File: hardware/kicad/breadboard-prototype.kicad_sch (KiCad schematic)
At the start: 12 parts, among them J1 nRF52 DK PCA10040 interface, J2 Waveshare 2.13inch HAT Rev2.1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, J3 Adafruit LIS3DH breakout, J4 DCF-1060N-800 (PON active-low), Q1 2N3904

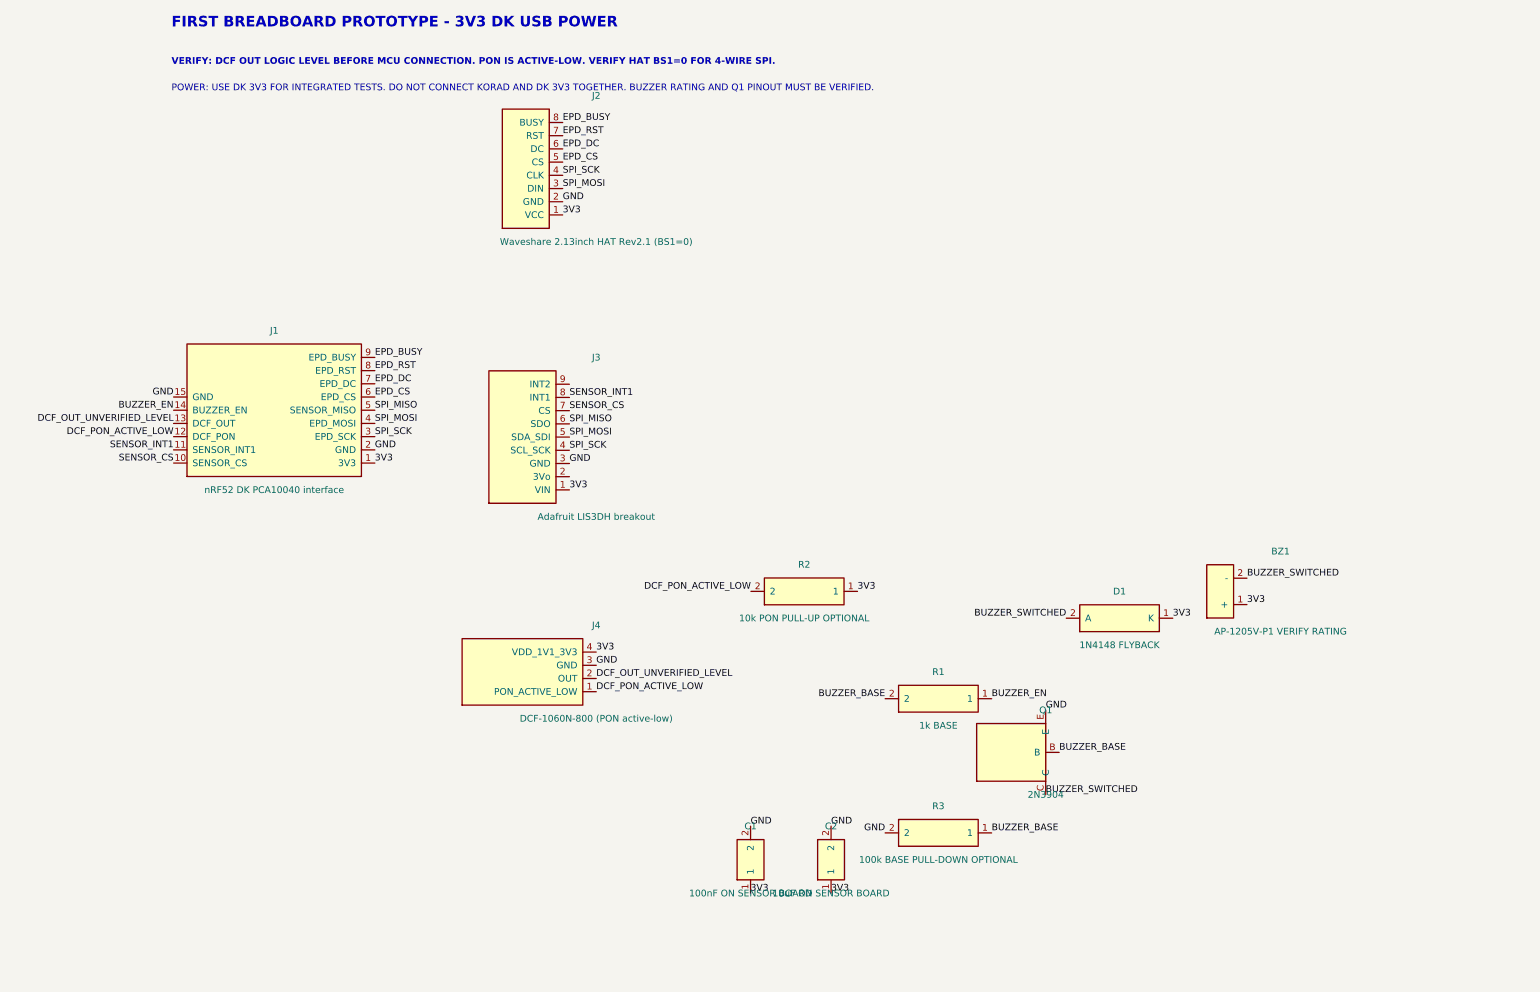
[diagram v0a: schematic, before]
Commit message: hardware: wire breadboard prototype modules
Add visible orthogonal wiring for module interfaces, DCF control,\nand the transistor-driven buzzer circuit.
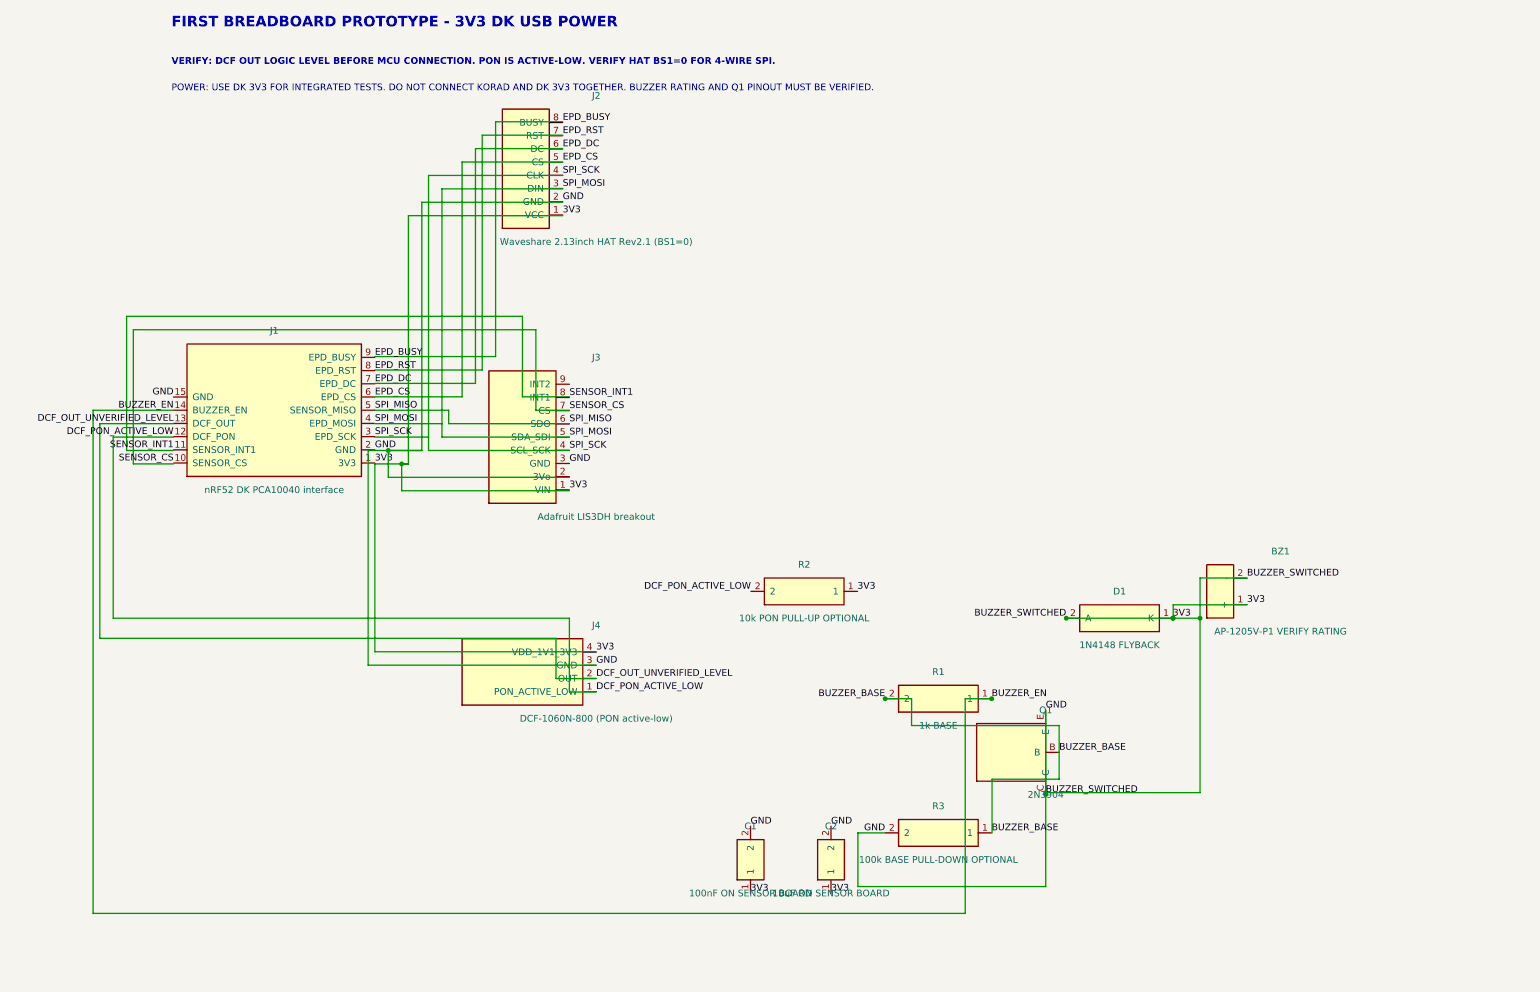
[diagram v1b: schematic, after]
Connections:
- net BUZZER_SWITCHED is gone; now on net 3V3: BZ1.2 (-), D1.2 (A), Q1.C

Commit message: hardware: tidy breadboard schematic layout
Rearrange modules into functional blocks, remove crossing routes,\nand export a reviewed PDF with cleaner display and buzzer wiring.
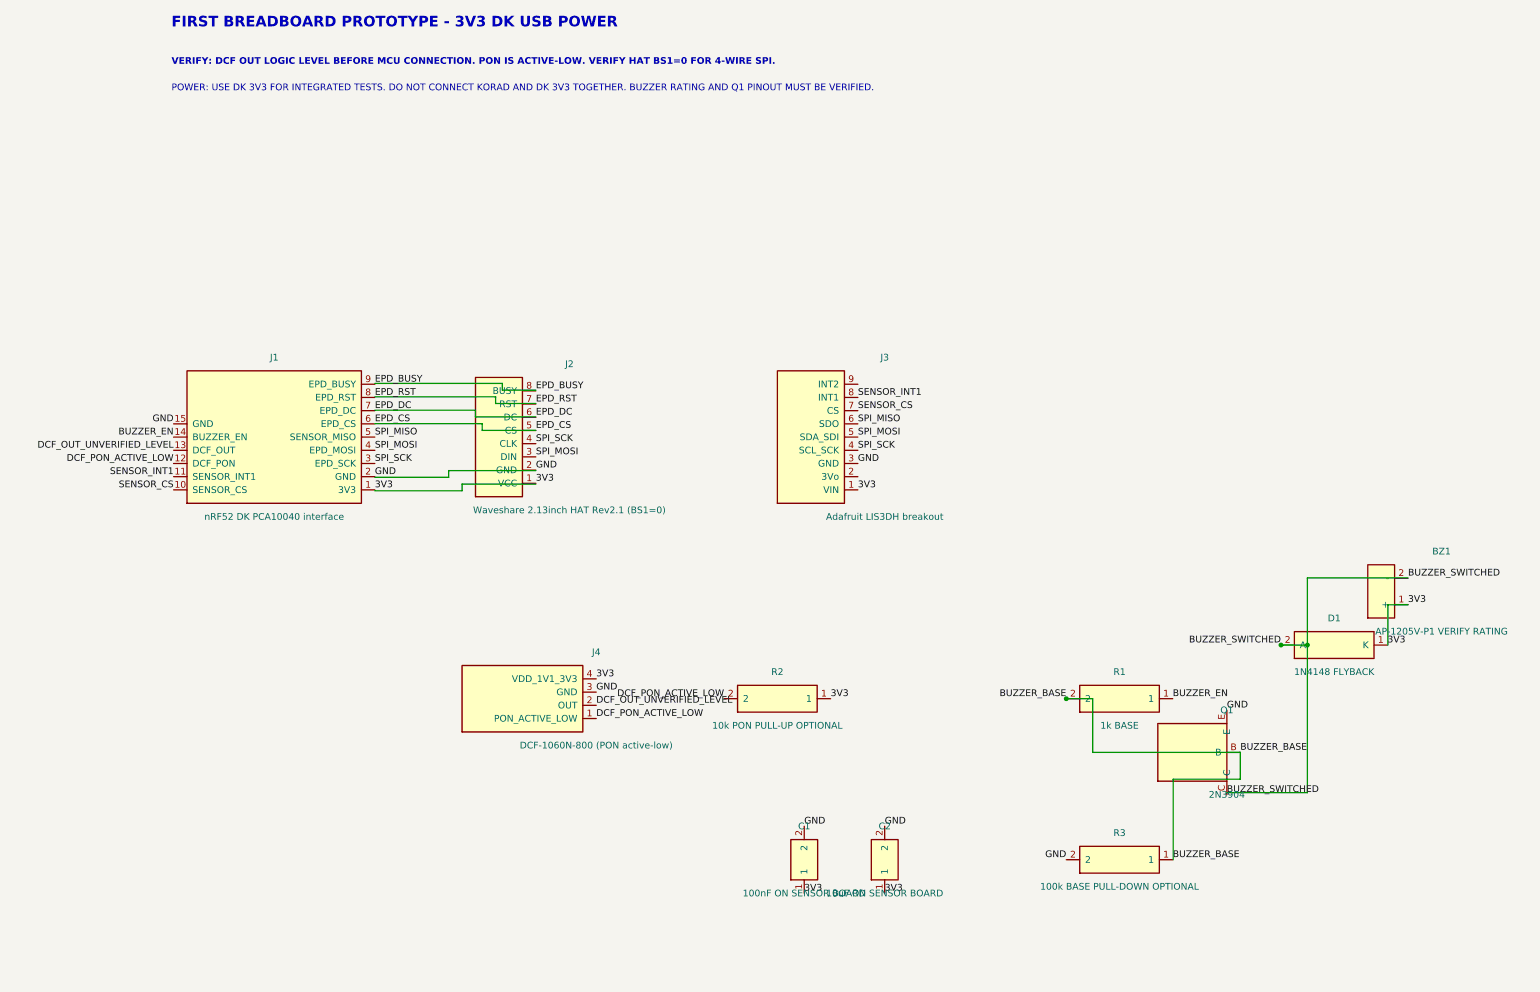
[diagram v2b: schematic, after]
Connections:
- net 3V3: no longer BZ1.2 (-), D1.2 (A), Q1.C
- new net BUZZER_SWITCHED: BZ1.2 (-), D1.2 (A), Q1.C
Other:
- moved on the sheet: BZ1, C1, C2, D1, J1, J2, J3, J4, Q1, R1, R2, R3

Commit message: hardware: modularize and clean breadboard schematic layout
Restructure schematic into five clearly demarcated functional blocks:
- Block 1: Host MCU Interface (nRF52 DK / PCA10040)
- Block 2: Display Interface (Waveshare 2.13" HAT Rev2.1)
- Block 3: Motion Sensor (Adafruit LIS3DH #2809) with decoupling
- Block 4: Time Sync (DCF-1060N-800) with PON pull-up and voltage caution
- Block 5: Transistor Buzzer Driver (2N3904 + 1N4148 + AP-1205V-P1)
- Block 6: Safety rules, boot safe states, and staged bring-up guide

Rebuild custom symbols on a strict 2.54 mm grid, register official KiCad
Device and power symbol libraries, eliminate long crossing wires, and export
reviewed PDF.
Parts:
- removed BZ1: AP-1205V-P1 VERIFY RATING, symbol BreadboardPrototype:Buzzer
- removed C1: 100nF ON SENSOR BOARD, symbol BreadboardPrototype:Capacitor
- removed C2: 10uF ON SENSOR BOARD, symbol BreadboardPrototype:Capacitor
- removed D1: 1N4148 FLYBACK, symbol BreadboardPrototype:Diode
- removed J1: nRF52 DK PCA10040 interface, symbol BreadboardPrototype:DK_Interface
- removed J2: Waveshare 2.13inch HAT Rev2.1 (BS1=0), symbol BreadboardPrototype:Epaper_HAT
- removed J3: Adafruit LIS3DH breakout, symbol BreadboardPrototype:LIS3DH_Breakout
- removed Q1: 2N3904, symbol BreadboardPrototype:NPN_2N3904
- removed R1: 1k BASE, symbol BreadboardPrototype:Resistor
- removed R2: 10k PON PULL-UP OPTIONAL, symbol BreadboardPrototype:Resistor
- removed R3: 100k BASE PULL-DOWN OPTIONAL, symbol BreadboardPrototype:Resistor
- added BZ1: AP-1205V-P1, symbol Device:Buzzer
- added C1: 100nF, symbol Device:C
- added C2: 10uF, symbol Device:C
- added D1: 1N4148, symbol Device:D
- added J1: nRF52 DK (PCA10040), symbol BreadboardPrototype:DK_PCA10040
- added J2: Waveshare 2.13in HAT Rev2.1, symbol BreadboardPrototype:Waveshare_2v1_HAT
- added J3: Adafruit LIS3DH (#2809), symbol BreadboardPrototype:Adafruit_LIS3DH
- added Q1: 2N3904, symbol Transistor_BJT:2N3904
- added R1: 1k, symbol Device:R
- added R2: 10k (OPT), symbol Device:R
- added R3: 100k (OPT), symbol Device:R
- J4: value DCF-1060N-800 (PON active-low) -> DCF-1060N-800
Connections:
- net 3V3 is gone; now on net GND: J4.4 (VDD)
- net BUZZER_EN: now also J1.6 (P0.17_EPD_CS), R1.1
- net EPD_BUSY: now also J1.11 (P0.23_SENSOR_INT1), J2.1 (VCC)
- net EPD_CS: now also J1.14 (P0.12_BUZZER_EN), J2.4 (CLK)
- net EPD_DC: now also J1.13 (P0.25_DCF_OUT), J2.3 (DIN)
- net EPD_RST: now also J1.12 (P0.24_DCF_PON), J2.2 (GND)
- net GND: now also C1.2, C2.2, J1.3 (P0.13_SCK), J2.7 (RST), J3.7 (CS), R3.2; no longer J4.3 (GND)
- net SENSOR_CS: now also J1.10 (P0.21_SENSOR_CS), J3.3 (GND)
- net SENSOR_INT1: now also J1.9 (P0.20_EPD_BUSY), J3.2 (3Vo)
- net SPI_MISO: now also J1.4 (P0.15_MOSI), J3.4 (SCL_SCK)
- net SPI_MOSI: now also J1.5 (P0.14_MISO), J2.6 (DC), J3.5 (SDA_SDI)
- net SPI_SCK: now also J1.15 (GND), J2.5 (CS), J3.6 (SDO)
- net DCF_OUT_UNVERIFIED_LEVEL renamed DCF_PON
- net DCF_PON: now also J1.8 (P0.19_EPD_RST), R2.2
- net DCF_PON_ACTIVE_LOW renamed DCF_OUT
- net DCF_OUT: now also J1.7 (P0.18_EPD_DC)
- new net: R1.2, R3.1
- new net +3V3: BZ1.1 (+), C1.1, C2.1, D1.2 (A), J2.8 (BUSY), J3.9 (INT2), J4.3 (GND), R2.1
- no-connect marks 0 -> 2
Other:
- note added: "(C1, C2 on breakout)"
- note added: "1. POWER: Power prototype solely from DK 3V3 rail via USB. NEVER connect KORAD bench supply and DK 3V3 rail together!"
- note added: "2. SAFE CONTROL STATES: Set DCF_PON HIGH (disabled, 0.0uA). Set EPD_CS and SENSOR_CS HIGH (unselected). Set BUZZER_EN LOW (off)."
- note added: "3. DCF-77 VERIFICATION: Measure DCF OUT high-level voltage before connecting to DK P0.25. Orient antenna perpendicular to Frankfurt."
- note added: "4. E-PAPER CONFIGURATION: Verify switch BS1 = 0 on back of Waveshare HAT for 4-wire SPI mode before powering display rail."
- note added: "5. BUZZER DRIVER: Verify 2N3904 TO-92 pinout (1=Emitter, 2=Base, 3=Collector). Diode D1 cathode connects to +3V3 to clamp flyback spikes."
- note added: "6. STAGED BRING-UP: 1) DK Blinky -> 2) E-Paper Demo -> 3) LIS3DH WHO_AM_I -> 4) DCF Standalone -> 5) DCF Sync -> 6) Buzzer Alarm."
- note added: "BLOCK 1: HOST CONTROLLER INTERFACE (nRF52 DK / PCA10040)"
- note added: "BLOCK 2: DISPLAY INTERFACE (Waveshare 2.13in HAT)"
- note added: "BLOCK 3: MOTION SENSOR (Adafruit LIS3DH #2809)"
- note added: "BLOCK 4: TIME SYNC (DCF-1060N-800 Module)"
- note added: "BLOCK 5: AUDIBLE ALARM (Transistor Buzzer Driver)"
- note added: "MEASURE OUT HIGH LEVEL BEFORE CONNECTING DK P0.25!"
- note added: "PON = 0V: Enabled (~68 uA) | PON = 3.3V: Disabled (0.0 uA)"
- note added: "PROTOTYPE SAFETY & INTEGRATION RULES"
- note added: "Verify BS1 = 0 (4-wire SPI) on HAT rear switch"
- note added: "Verify buzzer polarity & rating (<100mA)"
- note removed: "FIRST BREADBOARD PROTOTYPE - 3V3 DK USB POWER"
- note removed: "POWER: USE DK 3V3 FOR INTEGRATED TESTS. DO NOT CONNECT KORAD AND DK 3V3 TOGETHER. BUZZER RATING AND Q1 PINOUT MUST BE VERIFIED."
- note removed: "VERIFY: DCF OUT LOGIC LEVEL BEFORE MCU CONNECTION. PON IS ACTIVE-LOW. VERIFY HAT BS1=0 FOR 4-WIRE SPI."
- company: (none) -> Bachelor Thesis (APD)
- title: (none) -> Ultra-Low-Power Bedside Clock — Breadboard Prototype

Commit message: hardware: match schematic DK pins to updated guide
Rename DK symbol pins to P1_VDD/P1_GND/P4_GND and the new P0.xx map, and
point the power safety note at P1 VDD.

The netlist showed the 18a9166 schematic was electrically wrong: the
generator used y-down pin coordinates, so all four custom symbols were
mirrored vertically and every label hit the wrong pin (e.g. SPI_SCK on
GND). Flip their pin Y. Also embed the Q_NPN_EBC body for 2N3904 (Q1 had
no pins), un-mirror Q1, and reorient D1 and BZ1 so the flyback diode and
buzzer sit between +3V3 and the collector. ERC: 22 -> 1 (library-copy
warning for the flattened 2N3904).
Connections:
- net +3V3: now also D1.1 (K), J1.1 (P1_VDD), J2.1 (VCC), J3.1 (VIN), J4.4 (VDD); no longer D1.2 (A), J2.8 (BUSY), J3.9 (INT2), J4.3 (GND)
- net BUZZER_EN: now also J1.14 (P0.31_BUZZER_EN); no longer J1.6 (P0.17_EPD_CS)
- net DCF_OUT: now also J1.13 (P0.25_DCF_OUT), J4.2 (OUT); no longer J1.7 (P0.18_EPD_DC), J4.1 (PON)
- net DCF_PON: now also J1.12 (P0.24_DCF_PON), J4.1 (PON); no longer J1.8 (P0.19_EPD_RST), J4.2 (OUT)
- net EPD_BUSY: now also J1.9 (P0.29_EPD_BUSY), J2.8 (BUSY); no longer J1.11 (P0.23_SENSOR_INT1), J2.1 (VCC)
- net EPD_CS: now also J1.6 (P0.11_EPD_CS), J2.5 (CS); no longer J1.14 (P0.12_BUZZER_EN), J2.4 (CLK)
- net EPD_DC: now also J1.7 (P0.12_EPD_DC), J2.6 (DC); no longer J1.13 (P0.25_DCF_OUT), J2.3 (DIN)
- net EPD_RST: now also J1.8 (P0.28_EPD_RST), J2.7 (RST); no longer J1.12 (P0.24_DCF_PON), J2.2 (GND)
- net GND: now also J1.15 (P4_GND), J1.2 (P1_GND), J2.2 (GND), J3.3 (GND), J4.3 (GND), Q1.1 (E); no longer J1.3 (P0.13_SCK), J2.7 (RST), J3.7 (CS), J4.4 (VDD)
- net SENSOR_CS: now also J3.7 (CS); no longer J3.3 (GND)
- net SENSOR_INT1: now also J1.11 (P0.23_SENSOR_INT1), J3.8 (INT1); no longer J1.9 (P0.20_EPD_BUSY), J3.2 (3Vo)
- net SPI_MISO: now also J1.5 (P0.02_SPI_MISO), J3.6 (SDO); no longer J1.4 (P0.15_MOSI), J3.4 (SCL_SCK)
- net SPI_MOSI: now also J1.4 (P0.04_SPI_MOSI), J2.3 (DIN); no longer J1.5 (P0.14_MISO), J2.6 (DC)
- net SPI_SCK: now also J1.3 (P0.03_SPI_SCK), J2.4 (CLK), J3.4 (SCL_SCK); no longer J1.15 (GND), J2.5 (CS), J3.6 (SDO)
- net at BZ1.2 (-): now also D1.2 (A), Q1.3 (C)
- net at R1.2, R3.1: now also Q1.2 (B)
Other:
- note added: "1. POWER: Feed the 3V3 rail only from DK header P1 pin VDD (USB powered). Never use 5V, External supply, VDD_nRF or P22. NEVER connect KORAD bench supply and the 3V3 rail together!"
- note removed: "1. POWER: Power prototype solely from DK 3V3 rail via USB. NEVER connect KORAD bench supply and DK 3V3 rail together!"
- moved on the sheet: BZ1, D1
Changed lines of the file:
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@@
 	(polyline (pts (xy 15.24 158.75) (xy 281.94 158.75) (xy 281.94 198.12) (xy 15.24 198.12) (xy 15.24 158.75)) (stroke (width 0.254) (type default)) (fill (type none)))
 	(text "PROTOTYPE SAFETY & INTEGRATION RULES" (at 17.78 163.83 0) (effects (font (size 1.778 1.778) (bold yes)) (justify left bottom)))
-	(text "1. POWER: Power prototype solely from DK 3V3 rail via USB. NEVER connect KORAD bench supply and DK 3V3 rail together!" (at 17.78 168.91 0) (effects (font (size 1.2 1.2)) (justify left bottom)))
+	(text "1. POWER: Feed the 3V3 rail only from DK header P1 pin VDD (USB powered). Never use 5V, External supply, VDD_nRF or P22. NEVER connect KORAD bench supply and the 3V3 rail together!" (at 17.78 168.91 0) (effects (font (size 1.2 1.2)) (justify left bottom)))
 	(text "2. SAFE CONTROL STATES: Set DCF_PON HIGH (disabled, 0.0uA). Set EPD_CS and SENSOR_CS HIGH (unselected). Set BUZZER_EN LOW (off)." (at 17.78 173.99 0) (effects (font (size 1.2 1.2)) (justify left bottom)))
 	(text "3. DCF-77 VERIFICATION: Measure DCF OUT high-level voltage before connecting to DK P0.25. Orient antenna perpendicular to Frankfurt." (at 17.78 179.07 0) (effects (font (size 1.2 1.2)) (justify left bottom)))
@@
 	(wire (pts (xy 208.28 140.97) (xy 208.28 143.51)))
 	(label "GND" (at 208.28 143.51 270) (effects (font (size 1.27 1.27)) (justify right bottom)))
-	(symbol (lib_id "Transistor_BJT:2N3904") (at 218.44 127.0 0) (mirror y) (unit 1) (in_bom yes) (on_board yes) (dnp no)
+	(symbol (lib_id "Transistor_BJT:2N3904") (at 218.44 127.0 0) (unit 1) (in_bom yes) (on_board yes) (dnp no)
 		(property "Reference" "Q1" (at 223.52 124.46 0) (effects (font (size 1.27 1.27))))
 		(property "Value" "2N3904" (at 223.52 129.54 0) (effects (font (size 1.27 1.27))))
@@
 	(junction (at 236.22 119.38) (diameter 0))
 	(junction (at 248.92 119.38) (diameter 0))
-	(symbol (lib_id "Device:D") (at 236.22 113.03 90) (unit 1) (in_bom yes) (on_board yes) (dnp no)
+	(symbol (lib_id "Device:D") (at 236.22 113.03 270) (unit 1) (in_bom yes) (on_board yes) (dnp no)
 		(property "Reference" "D1" (at 232.41 113.03 90) (effects (font (size 1.27 1.27))))
 		(property "Value" "1N4148" (at 240.03 113.03 90) (effects (font (size 1.27 1.27))))
@@
 	(wire (pts (xy 236.22 116.84) (xy 236.22 119.38)))
 	(wire (pts (xy 236.22 109.22) (xy 236.22 106.68)))
-	(symbol (lib_id "Device:Buzzer") (at 246.38 113.03 270) (unit 1) (in_bom yes) (on_board yes) (dnp no)
+	(symbol (lib_id "Device:Buzzer") (at 251.46 113.03 0) (unit 1) (in_bom yes) (on_board yes) (dnp no)
 		(property "Reference" "BZ1" (at 252.73 110.49 0) (effects (font (size 1.27 1.27))))
 		(property "Value" "AP-1205V-P1" (at 252.73 115.57000000000001 0) (effects (font (size 1.27 1.27))))
